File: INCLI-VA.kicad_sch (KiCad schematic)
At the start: 0 parts

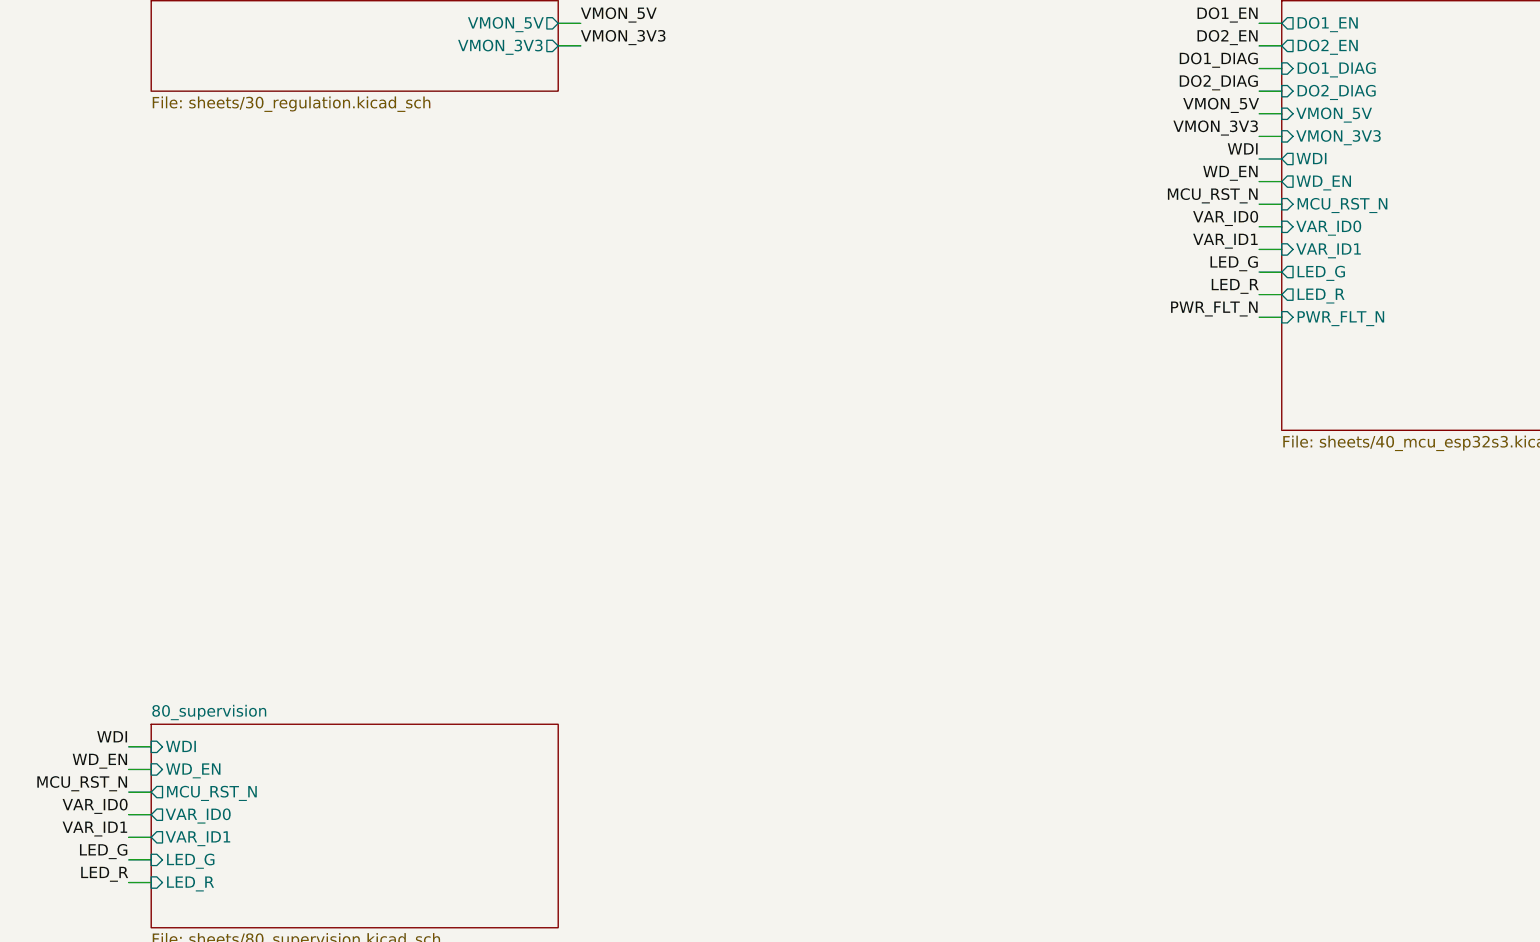
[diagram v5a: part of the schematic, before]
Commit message: [Claude Code] 80_supervision: TPS3828-33-Q1, LED y VAR_ID; J1/J2 verticales; contorno con muesca
- 80_supervision: U801 TPS3828-33QDBVRQ1 (supervisor de +3V3_D + watchdog,
  WDI <- IO17), R802 0 ohm, R801 DNP; LED verde/rojo DNP en PROD (caja
  opaca); VAR_ID0/1 (CAN/OUT) y VAR_ID2 (IO8, CABIN, DNP).
- WD_EN eliminado (IO18 libre); VAR_ID2 ocupa su pin en las hojas 40/80 y la raíz.
- 10_power_input: J1/J2 MSTBV 2,5 GF 5.08 verticales (1777109 / 1777073).
- lib: se borran los símbolos URB2405 y TPS7A1650; U101: vías del EP a Ø 0.45 mm.
- PCB: contorno único con muesca de 8 x 35 mm para la antena (antes, dos
  rectángulos superpuestos); serigrafía de U401 recortada en la muesca.
- ERC: 0 errores, 1 aviso intencional (U101_RTN).

Co-Authored-By: Claude Opus 5.5 <noreply@anthropic.com>
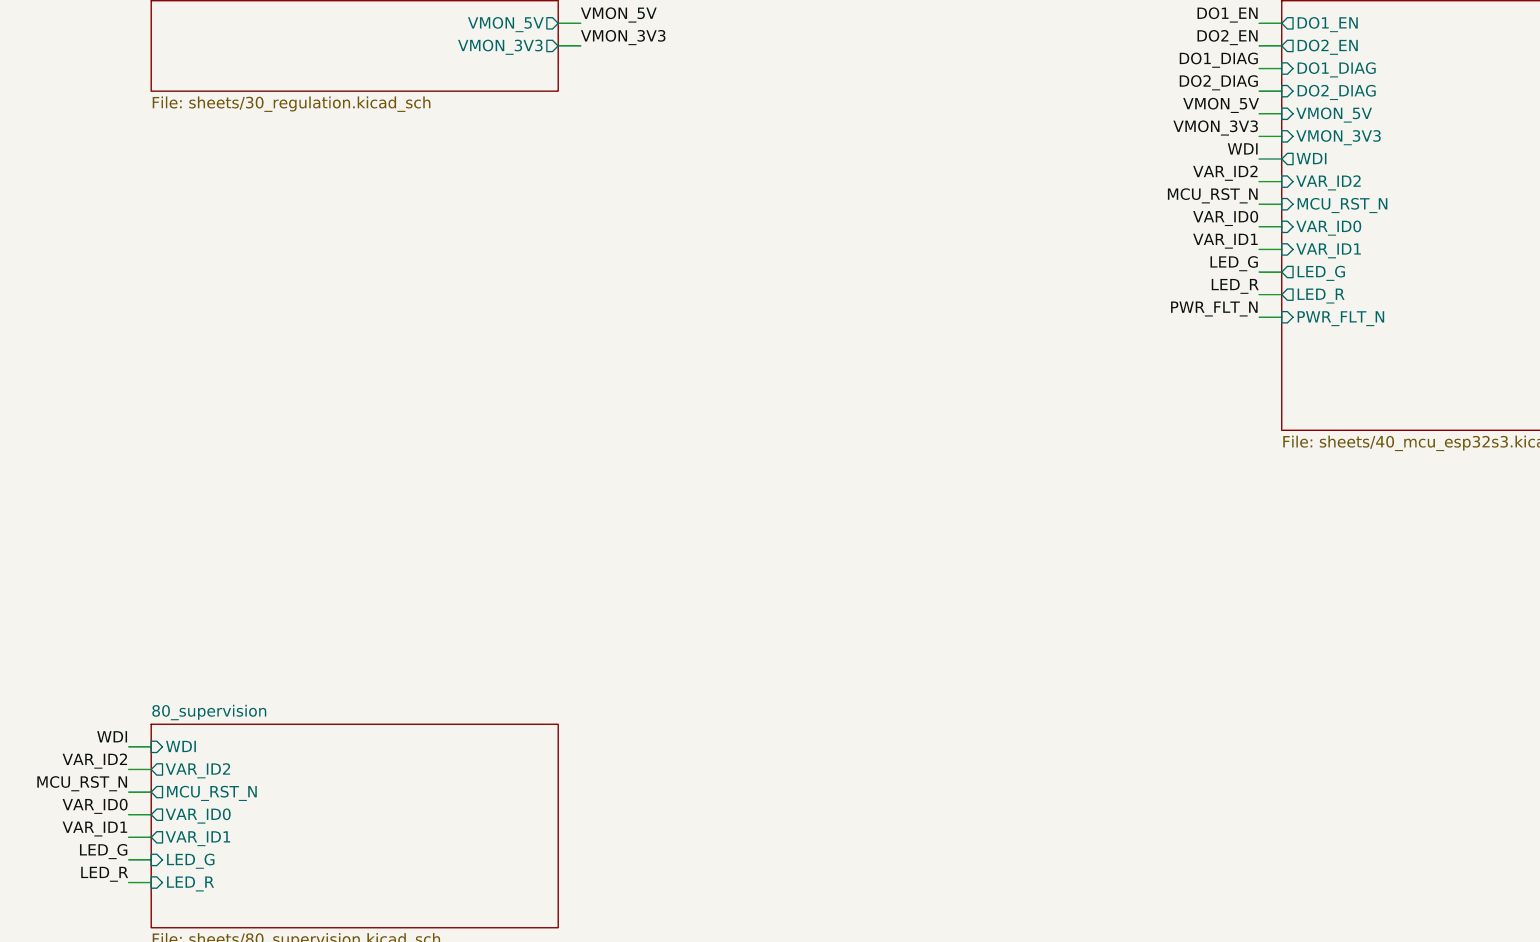
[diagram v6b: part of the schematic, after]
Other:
- sheet 40_mcu ports: added VAR_ID2; removed WD_EN
- sheet 80_supervision ports: added VAR_ID2; removed WD_EN
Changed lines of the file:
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@@
 		)
 	)
-	(label "WD_EN"
+	(label "VAR_ID2"
 		(at 154.94 144.78 180)
 		(effects
@@
 		)
 	)
-	(label "WD_EN"
+	(label "VAR_ID2"
 		(at 27.94 210.82 180)
 		(effects
@@
 			)
 		)
-		(pin "WD_EN" input
+		(pin "VAR_ID2" output
 			(at 30.48 210.82 180)
 			(effects
@@
 			)
 		)
-		(pin "WD_EN" output
+		(pin "VAR_ID2" input
 			(at 157.48 144.78 180)
 			(effects

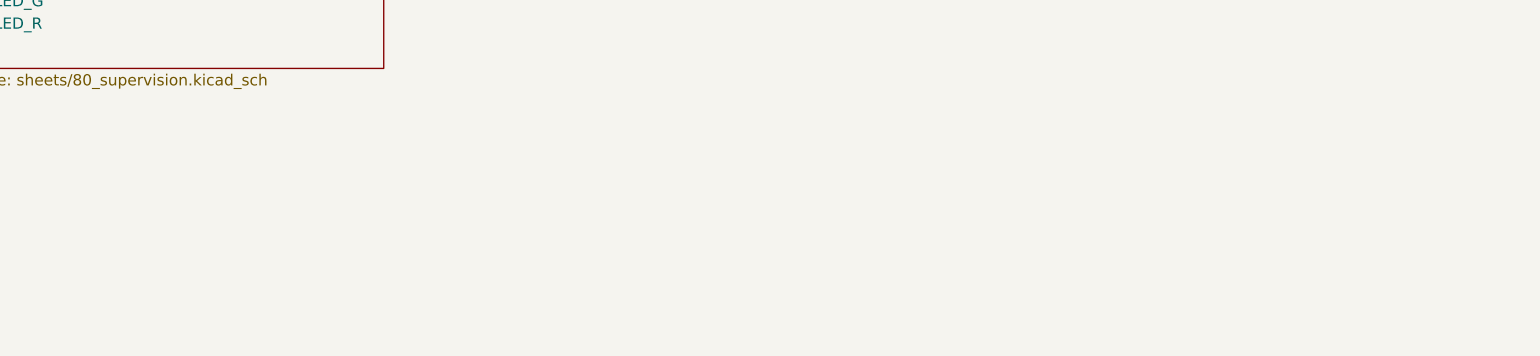
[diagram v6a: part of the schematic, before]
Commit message: [Claude Code] raíz: agujeros de fijación H1-H4 (M3, sin cobre) en el esquemático
Mechanical:MountingHole + MountingHole_3.2mm_M3 (NPTH, sin cobre), fuera
del BOM, para que Update PCB from Schematic no los vuelva a borrar. La
posición la define el layout.

Co-Authored-By: Claude Opus 5.5 <noreply@anthropic.com>
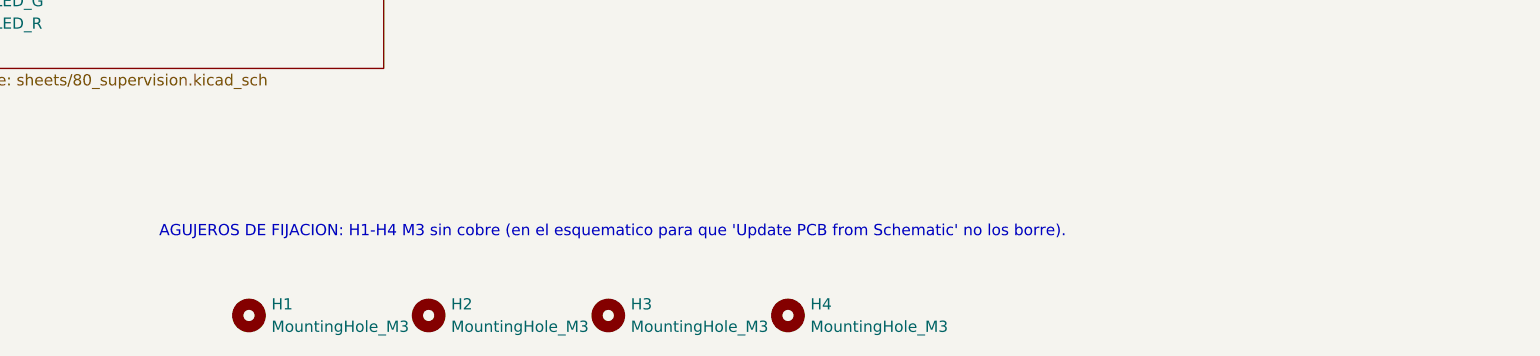
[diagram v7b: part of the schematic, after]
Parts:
- added H1, H2, H3, H4: MountingHole_M3, MountingHole:MountingHole_3.2mm_M3, symbol Mechanical:MountingHole
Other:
- note added: "AGUJEROS DE FIJACION: H1-H4 M3 sin cobre (en el esquematico para que 'Update PCB from Schematic' no los borre)."
